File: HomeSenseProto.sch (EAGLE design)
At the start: 18 parts, among them IC1 ESP12SMT

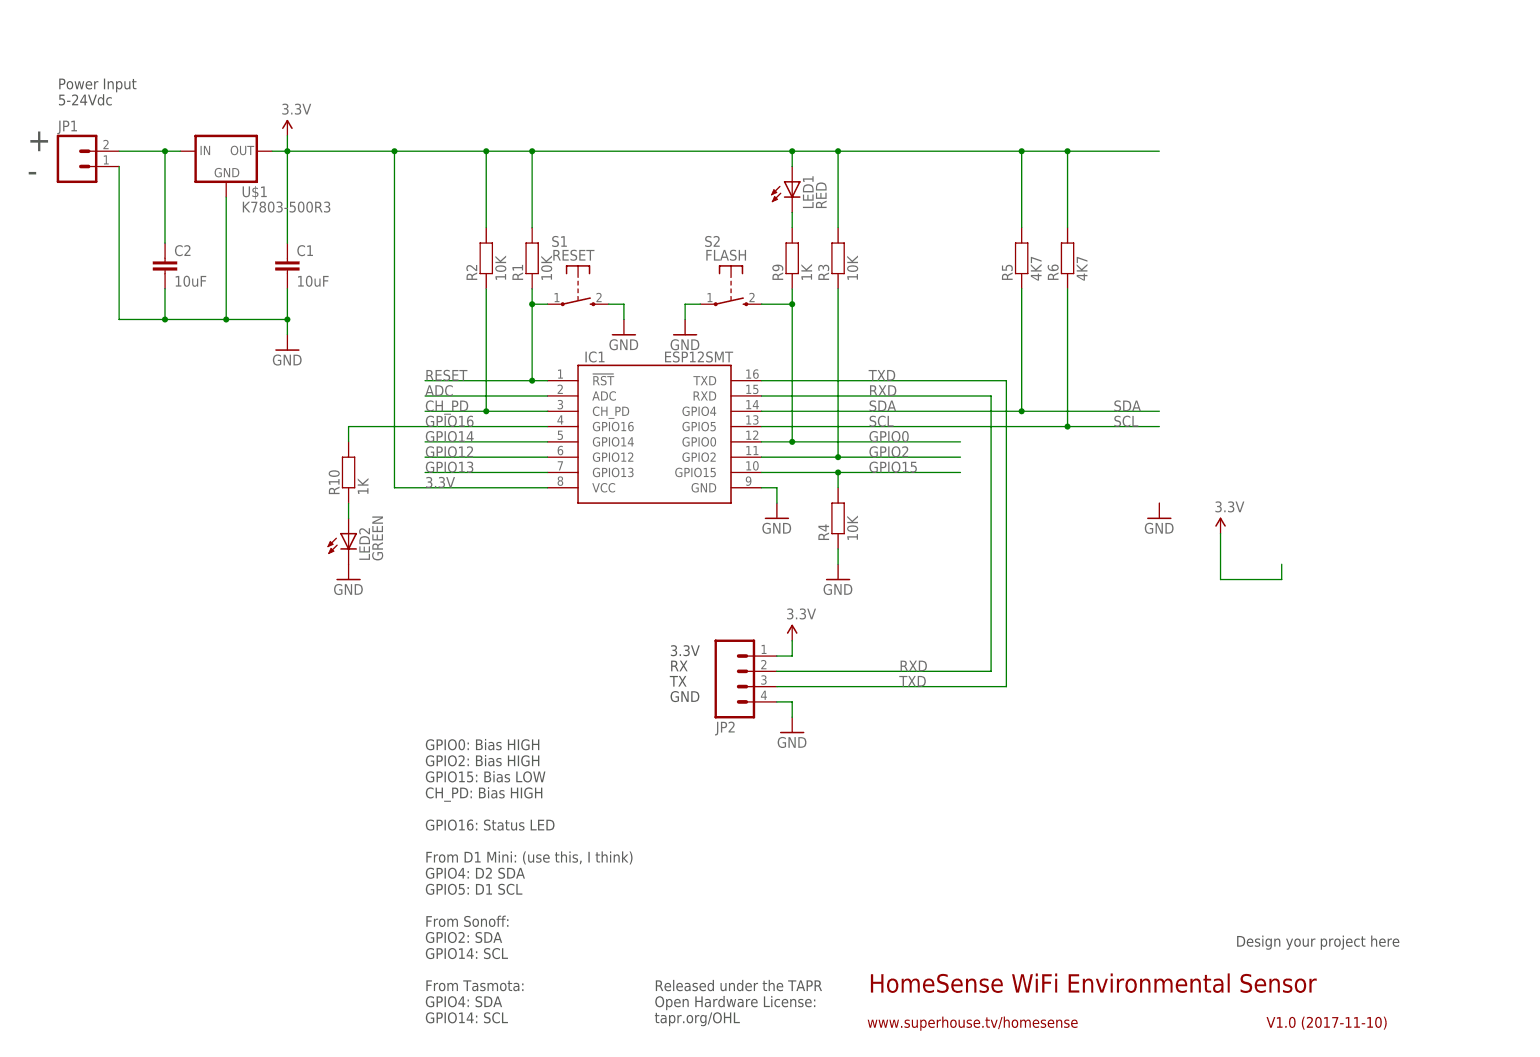
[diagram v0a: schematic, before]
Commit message: Added I2C header for proto area
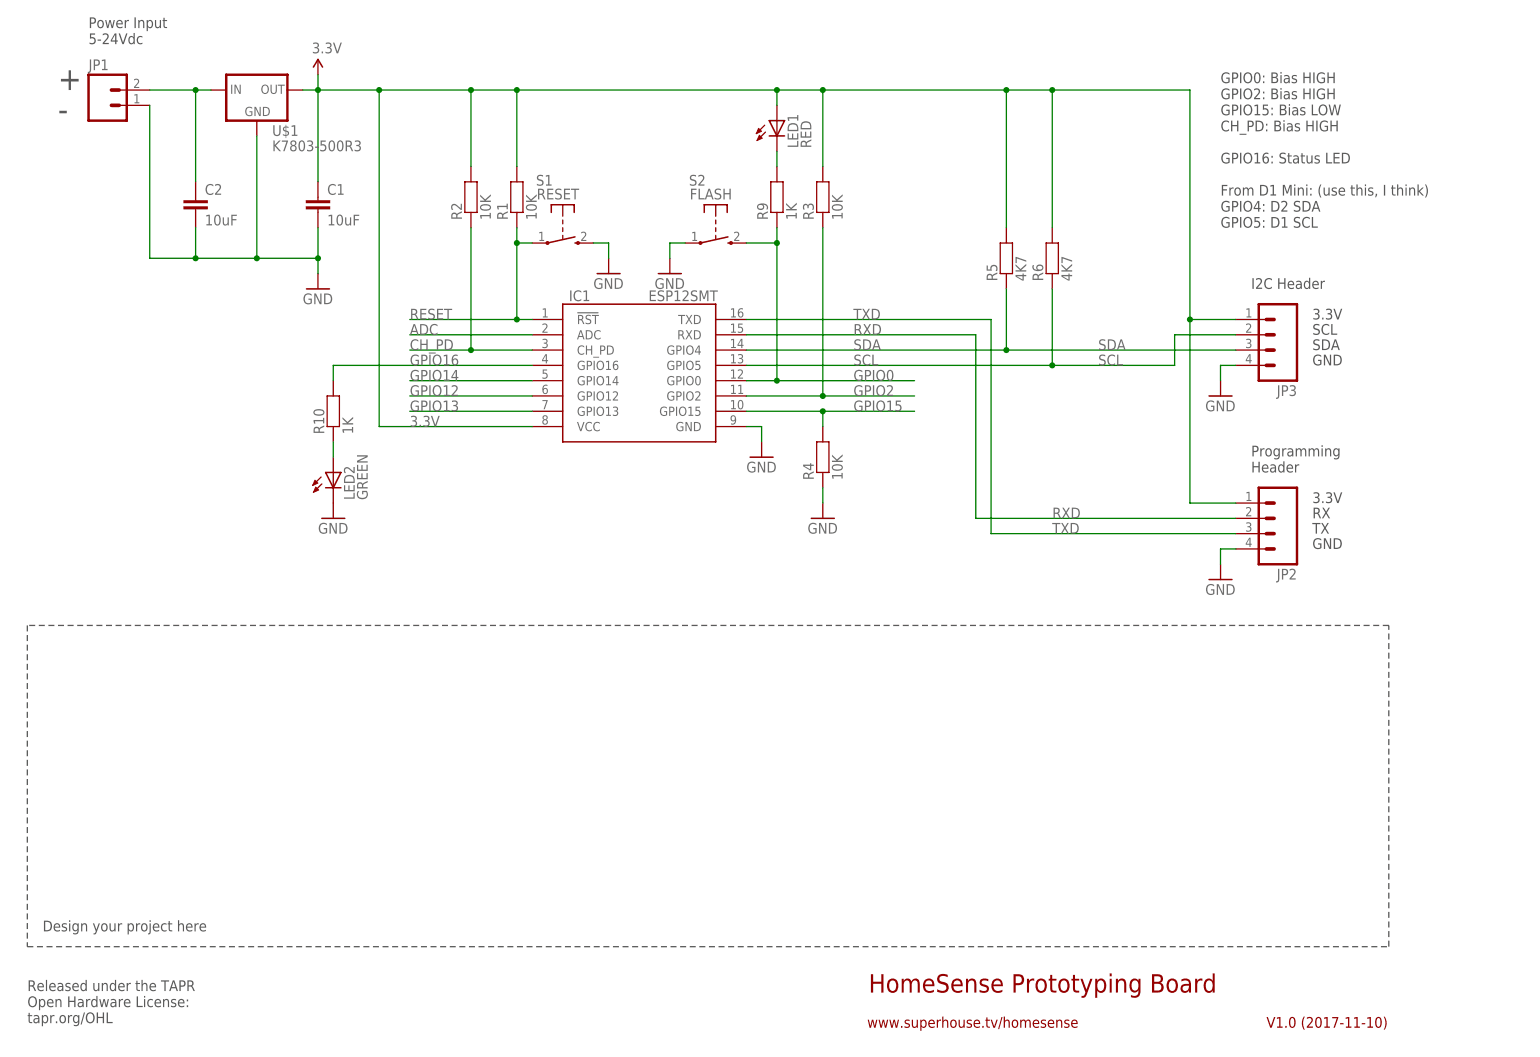
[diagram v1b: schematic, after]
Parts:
- added JP3: (no value), freetronics-jon:M04PTH
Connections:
- net 3.3V: now also JP3.1
- net GND: now also JP3.4
- net SCL: now also JP3.2
- net SDA: now also JP3.3
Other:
- note added: "GPIO0: Bias HIGH GPIO2: Bias HIGH GPIO15: Bias LOW CH_PD: Bias HIGH GPIO16: Status LED From D1 Mini: (use this, I think) GPIO4: D2 SDA GPIO5: D1 SCL"
- note added: "HomeSense Prototyping Board"
- note added: "I2C Header"
- note added: "Programming Header"
- note added: "SCL"
- note added: "SDA"
- note removed: "GPIO0: Bias HIGH GPIO2: Bias HIGH GPIO15: Bias LOW CH_PD: Bias HIGH GPIO16: Status LED From D1 Mini: (use this, I think) GPIO4: D2 SDA GPIO5: D1 SCL From Sonoff: GPIO2: SDA GPIO14: SCL From Tasmota: GPIO4: SDA GPIO14: SCL"
- note removed: "HomeSense WiFi Environmental Sensor"
- moved on the sheet: C1, C2, IC1, JP1, JP2, LED1, LED2, R1, R10, R2, R3, R4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

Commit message: Routing tweaks
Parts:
- added LED3: GREEN, freetronics-jon:LED0603
- renumbered U$1 to REG1
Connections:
- net GND: now also LED3.C
- net N$11: now also LED3.A
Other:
- note added: "A0"
- note added: "D0"
- note added: "D1"
- note added: "D2"
- note added: "D3"
- note added: "D4"
- note added: "D5"
- note added: "D6"
- note added: "D7"
- note added: "D8"
- note added: "GPIO0: Bias HIGH GPIO2: Bias HIGH GPIO15: Bias LOW CH_PD: Bias HIGH From D1 Mini: GPIO4: D2 SDA GPIO5: D1 SCL GPIO16: D0 Status LED"
- note added: "I2C pullups"
- note added: "Note: Only fit one of LED2 or LED3, not both. LED2 is on the top of the PCB, LED3 is on the bottom. Place at LED2 position by default. The LED3 position can be used if the LED must be externally visible, by drilling a hole through the case."
- note added: "SKU: HSPROTO"
- note added: "V1.0 (2018-02-15)"
- note added: "www.superhouse.tv/hsproto"
- note removed: "GPIO0: Bias HIGH GPIO2: Bias HIGH GPIO15: Bias LOW CH_PD: Bias HIGH GPIO16: Status LED From D1 Mini: (use this, I think) GPIO4: D2 SDA GPIO5: D1 SCL"
- note removed: "V1.0 (2017-11-10)"
- note removed: "www.superhouse.tv/homesense"
- moved on the sheet: LED2, R5, R6
